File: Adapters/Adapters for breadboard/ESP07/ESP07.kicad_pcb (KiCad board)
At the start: 2 copper layers, 73.4 x 21.3 mm, 2 parts, among them J1 Conn_02x08_Counter_Clockwise

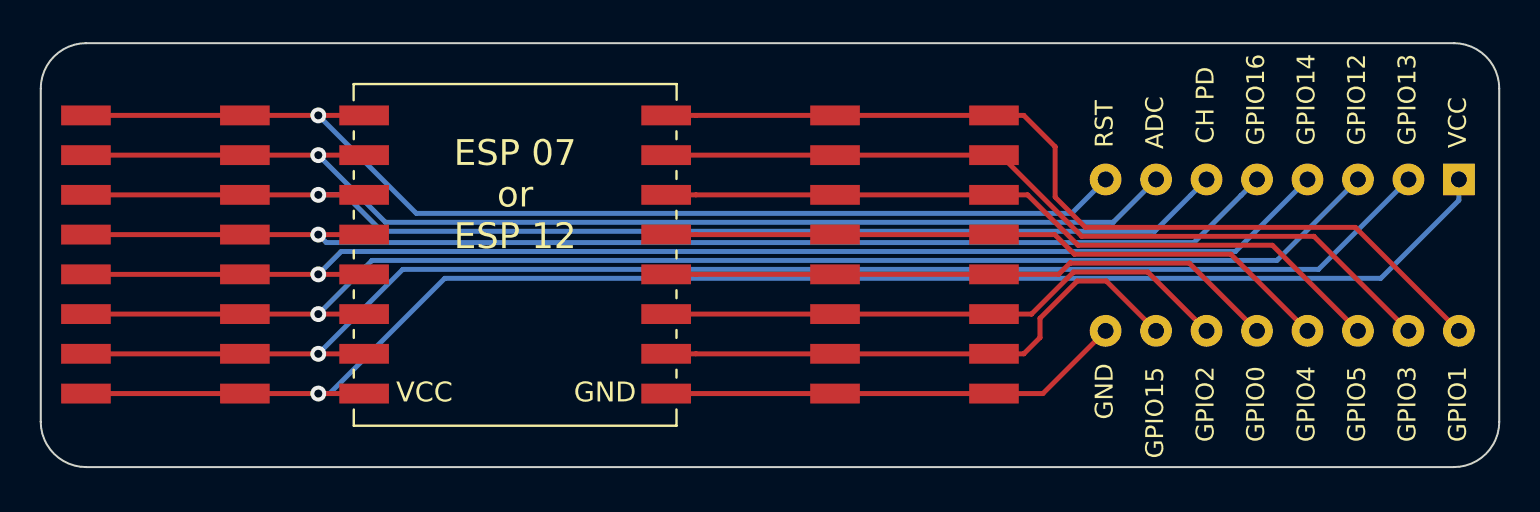
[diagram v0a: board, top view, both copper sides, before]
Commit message: Added the breadboard form of the ESP connector. Re-generated the Gerber for the adapter
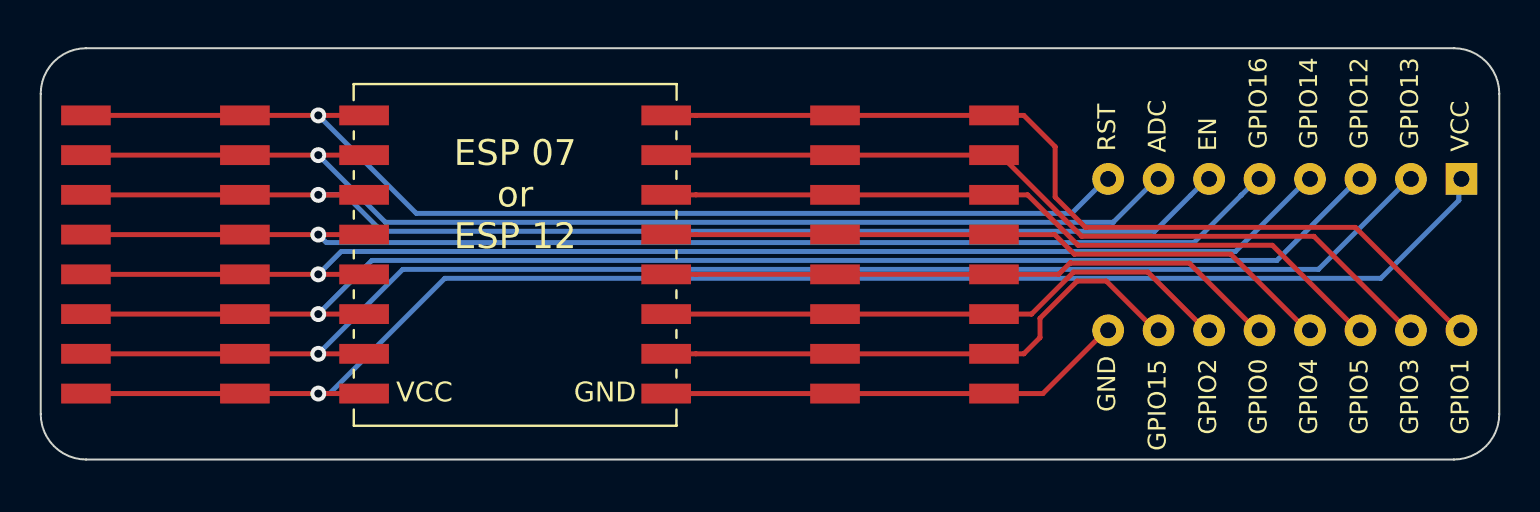
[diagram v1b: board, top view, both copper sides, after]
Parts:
- J1: footprint Package_DIP:DIP-16_W7.62mm -> ArduinoUnoMultiProgrammerAdapters:ESP07BreaboardSocket
- moved J1 10.9 mm to (189.9, 100.3), turned to 90 degrees
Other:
- board size 73.4 x 21.3 mm -> 73.4 x 20.7 mm
- board text removed: "ADC"
- board text removed: "CH PD"
- board text removed: "GND"
- board text removed: "GPIO0"
- board text removed: "GPIO1"
- board text removed: "GPIO12"
- board text removed: "GPIO13"
- board text removed: "GPIO14"
- board text removed: "GPIO15"
- board text removed: "GPIO16"
- board text removed: "GPIO2"
- board text removed: "GPIO3"
- board text removed: "GPIO4"
- board text removed: "GPIO5"
- board text removed: "RST"
- board text removed: "VCC"

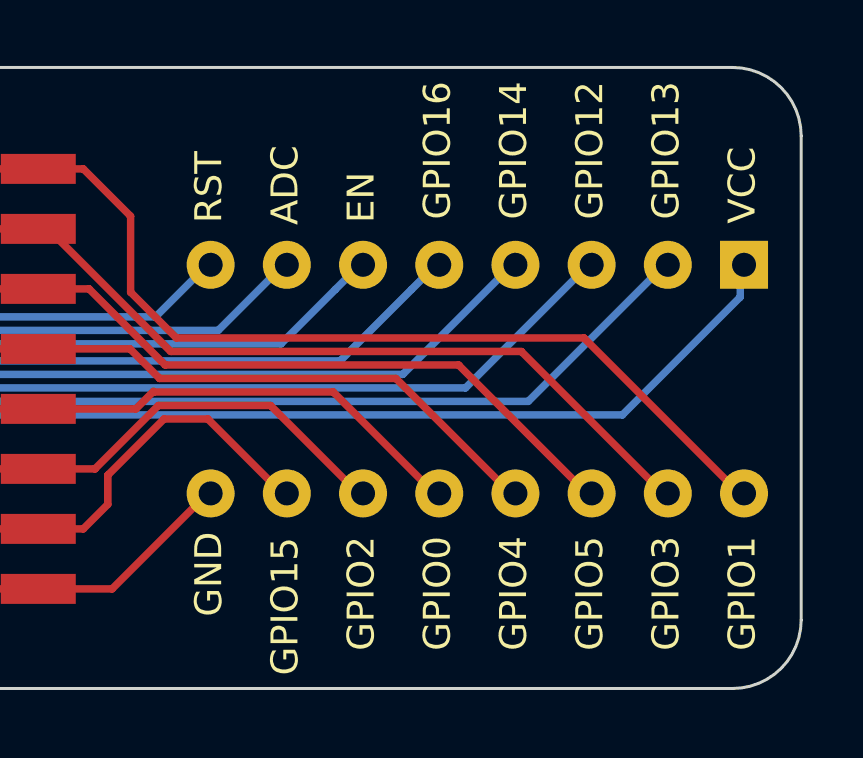
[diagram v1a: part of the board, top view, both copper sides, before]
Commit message: Fixed error in ESP breadboard adapter footprint, updated the schema to wire the for the new layout. Updated the ESP flashing adapter.
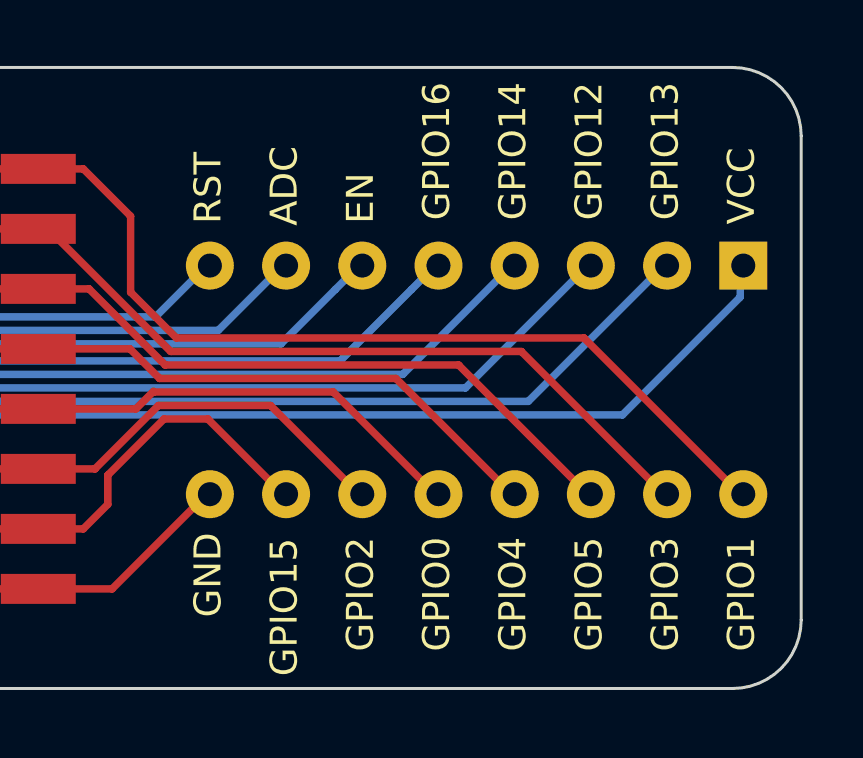
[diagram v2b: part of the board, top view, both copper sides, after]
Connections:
- J1 pad 1: Net-(ESP-7-Pad8) -> Net-(ESP-7-Pad1)
- J1 pad 2: Net-(ESP-7-Pad7) -> Net-(ESP-7-Pad2)
- J1 pad 3: Net-(ESP-7-Pad6) -> Net-(ESP-7-Pad3)
- J1 pad 4: Net-(ESP-7-Pad5) -> Net-(ESP-7-Pad4)
- J1 pad 5: Net-(ESP-7-Pad4) -> Net-(ESP-7-Pad5)
- J1 pad 6: Net-(ESP-7-Pad3) -> Net-(ESP-7-Pad6)
- J1 pad 7: Net-(ESP-7-Pad2) -> Net-(ESP-7-Pad7)
- J1 pad 8: Net-(ESP-7-Pad1) -> Net-(ESP-7-Pad8)
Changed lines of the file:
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@@
   )
   (module ArduinoUnoMultiProgrammerAdapters:ESP07BreaboardSocket (layer F.Cu)
-    (at 189.8904 100.33 90)
+    (at 189.865 100.3554 90)
     (descr "16-lead though-hole mounted DIP package, row spacing 7.62 mm (300 mils)")
     (tags "THT DIP DIL PDIP 2.54mm 7.62mm 300mil")
-    (fp_text reference J1 (at 0.0254 12.7186 270) (layer F.SilkS) hide
+    (fp_text reference J1 (at 0.3302 0.0762 270) (layer F.SilkS) hide
       (effects (font (size 1 1) (thickness 0.15)))
     )
@@
       (effects (font (size 0.9 0.9) (thickness 0.15)))
     )
-    (fp_text user %R (at 0.0254 1.4986 270) (layer F.Fab)
-      (effects (font (size 1 1) (thickness 0.15)))
-    )
     (fp_line (start -4.8646 11.9386) (end 4.9354 11.9386) (layer F.CrtYd) (width 0.05))
     (fp_line (start -4.8646 -8.9114) (end -4.8646 11.9386) (layer F.CrtYd) (width 0.05))
@@
     (pad 16 thru_hole oval (at -3.7846 10.3886 270) (size 1.6 1.6) (drill 0.8) (layers *.Cu *.Mask)
       (net 5 "Net-(ESP-7-Pad16)"))
-    (pad 8 thru_hole oval (at 3.8354 -7.3914 270) (size 1.6 1.6) (drill 0.8) (layers *.Cu *.Mask)
+    (pad 1 thru_hole oval (at 3.8354 -7.3914 270) (size 1.6 1.6) (drill 0.8) (layers *.Cu *.Mask)
       (net 11 "Net-(ESP-7-Pad1)"))
     (pad 15 thru_hole oval (at -3.7846 7.8486 270) (size 1.6 1.6) (drill 0.8) (layers *.Cu *.Mask)
       (net 4 "Net-(ESP-7-Pad15)"))
-    (pad 7 thru_hole oval (at 3.8354 -4.8514 270) (size 1.6 1.6) (drill 0.8) (layers *.Cu *.Mask)
+    (pad 2 thru_hole oval (at 3.8354 -4.8514 270) (size 1.6 1.6) (drill 0.8) (layers *.Cu *.Mask)
       (net 13 "Net-(ESP-7-Pad2)"))
     (pad 14 thru_hole oval (at -3.7846 5.3086 270) (size 1.6 1.6) (drill 0.8) (layers *.Cu *.Mask)
       (net 6 "Net-(ESP-7-Pad14)"))
-    (pad 6 thru_hole oval (at 3.8354 -2.3114 270) (size 1.6 1.6) (drill 0.8) (layers *.Cu *.Mask)
+    (pad 3 thru_hole oval (at 3.8354 -2.3114 270) (size 1.6 1.6) (drill 0.8) (layers *.Cu *.Mask)
       (net 15 "Net-(ESP-7-Pad3)"))
     (pad 13 thru_hole oval (at -3.7846 2.7686 270) (size 1.6 1.6) (drill 0.8) (layers *.Cu *.Mask)
       (net 7 "Net-(ESP-7-Pad13)"))
-    (pad 5 thru_hole oval (at 3.8354 0.2286 270) (size 1.6 1.6) (drill 0.8) (layers *.Cu *.Mask)
+    (pad 4 thru_hole oval (at 3.8354 0.2286 270) (size 1.6 1.6) (drill 0.8) (layers *.Cu *.Mask)
       (net 9 "Net-(ESP-7-Pad4)"))
     (pad 12 thru_hole oval (at -3.7846 0.2286 270) (size 1.6 1.6) (drill 0.8) (layers *.Cu *.Mask)
       (net 8 "Net-(ESP-7-Pad12)"))
-    (pad 4 thru_hole oval (at 3.8354 2.7686 270) (size 1.6 1.6) (drill 0.8) (layers *.Cu *.Mask)
+    (pad 5 thru_hole oval (at 3.8354 2.7686 270) (size 1.6 1.6) (drill 0.8) (layers *.Cu *.Mask)
       (net 10 "Net-(ESP-7-Pad5)"))
     (pad 11 thru_hole oval (at -3.7846 -2.3114 270) (size 1.6 1.6) (drill 0.8) (layers *.Cu *.Mask)
       (net 3 "Net-(ESP-7-Pad11)"))
-    (pad 3 thru_hole oval (at 3.8354 5.3086 270) (size 1.6 1.6) (drill 0.8) (layers *.Cu *.Mask)
+    (pad 6 thru_hole oval (at 3.8354 5.3086 270) (size 1.6 1.6) (drill 0.8) (layers *.Cu *.Mask)
       (net 12 "Net-(ESP-7-Pad6)"))
     (pad 10 thru_hole oval (at -3.7846 -4.8514 270) (size 1.6 1.6) (drill 0.8) (layers *.Cu *.Mask)
       (net 1 "Net-(ESP-7-Pad10)"))
-    (pad 2 thru_hole oval (at 3.8354 7.8486 270) (size 1.6 1.6) (drill 0.8) (layers *.Cu *.Mask)
+    (pad 7 thru_hole oval (at 3.8354 7.8486 270) (size 1.6 1.6) (drill 0.8) (layers *.Cu *.Mask)
       (net 16 "Net-(ESP-7-Pad7)"))
     (pad 9 thru_hole oval (at -3.7846 -7.3914 270) (size 1.6 1.6) (drill 0.8) (layers *.Cu *.Mask)
       (net 2 "Net-(ESP-7-Pad9)"))
-    (pad 1 thru_hole rect (at 3.8354 10.3886) (size 1.6 1.6) (drill 0.8) (layers *.Cu *.Mask)
+    (pad 8 thru_hole rect (at 3.8354 10.3886) (size 1.6 1.6) (drill 0.8) (layers *.Cu *.Mask)
       (net 14 "Net-(ESP-7-Pad8)"))
-    (model ${KISYS3DMOD}/Package_DIP.3dshapes/DIP-16_W7.62mm.wrl
-      (at (xyz 0 0 0))
-      (scale (xyz 1 1 1))
-      (rotate (xyz 0 0 0))
-    )
   )
   (module ArduinoUnoMultiProgrammerAdapters:ESP-07Socket (layer F.Cu)
